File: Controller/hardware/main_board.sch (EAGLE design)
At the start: 47 parts, among them IC1 LINEAR_78DT, IC2 40XX_4050D, IC3 LP298XS, IC5 ATMEGA328, U1 CSTNE16M0VH3L000R0, X1 MICROSD_SMD, X4 CON-PHOENIX-508_MST2V

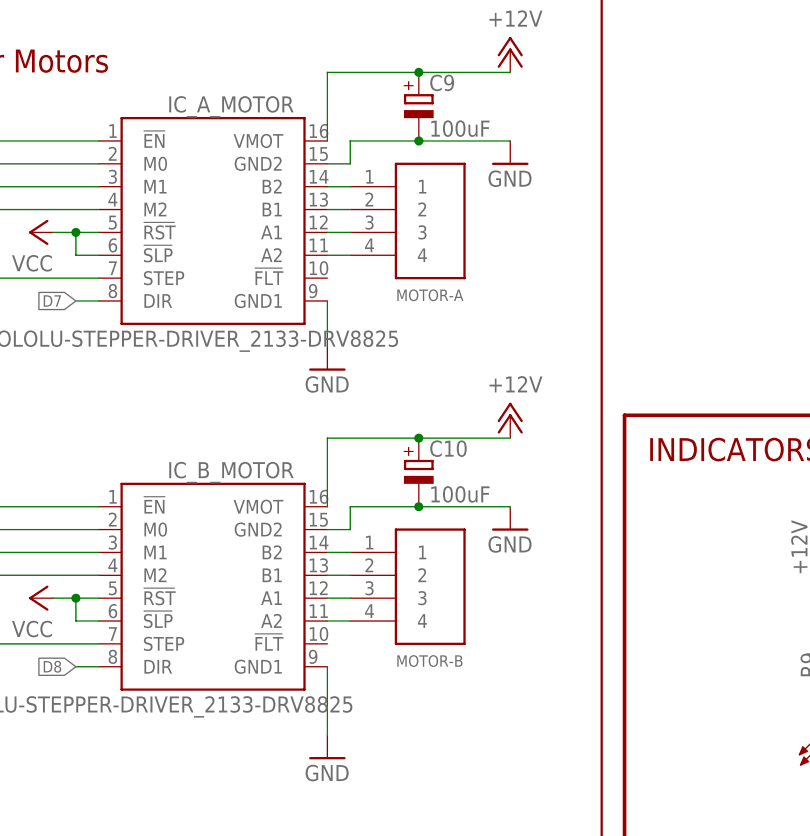
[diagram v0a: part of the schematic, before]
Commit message: changed motor connectors
changed motor connectors to .1" pitch 4 pos headers. the stepper motor stock connectors press nicely onto these. so if one wanted to they could just pins instead of soldering wires directly to the board. if soldering directly to the board the new larger pads should be more robust too.
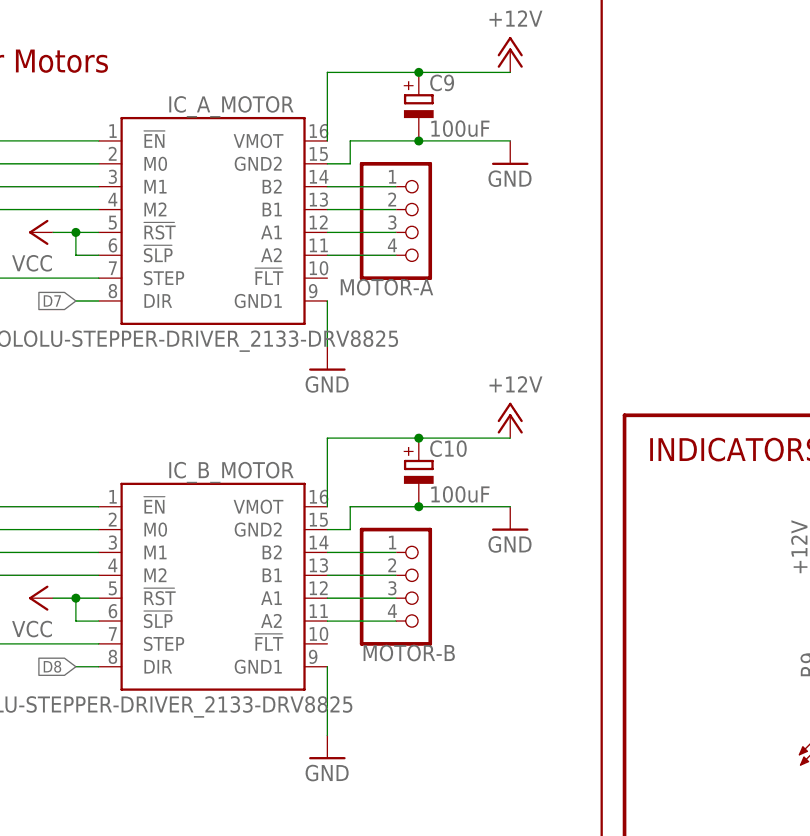
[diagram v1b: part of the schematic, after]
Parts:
- MOTOR-A, MOTOR-B: value JST_EPH_4PIN -> (none); device main_board:JST_EPH_4PIN -> main_board:PINHD-1X4
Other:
- moved on the sheet: MOTOR-A, MOTOR-B
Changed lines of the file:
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@@
 <part name="C9" library="main_board" deviceset="C100UF_EC" device="E3.5-8" value="100uF"/>
 <part name="C10" library="main_board" deviceset="C100UF_EC" device="E3.5-8" value="100uF"/>
-<part name="MOTOR-A" library="main_board" deviceset="JST_EPH_4PIN" device=""/>
-<part name="MOTOR-B" library="main_board" deviceset="JST_EPH_4PIN" device=""/>
 <part name="J1" library="main_board" deviceset="JUMPER_J2" device="X5MM"/>
 <part name="JP4" library="main_board" deviceset="JST_EPH_2PIN" device=""/>
@@
 <part name="C15" library="main_board" deviceset="C1.0UF_0805" device="0805" value="1.0uF"/>
 <part name="SUPPLY4" library="main_board" deviceset="GND" device=""/>
+<part name="MOTOR-A" library="main_board" deviceset="PINHD-1X4" device=""/>
+<part name="MOTOR-B" library="main_board" deviceset="PINHD-1X4" device=""/>
 </parts>
 <sheets>
@@
 <attribute name="VALUE" x="92.583" y="46.2026" size="1.778" layer="96"/>
 </instance>
-<instance part="MOTOR-A" gate="G$1" x="88.9" y="78.74" smashed="yes">
-<attribute name="NAME" x="88.9" y="68.58" size="1.27" layer="95"/>
-</instance>
-<instance part="MOTOR-B" gate="G$1" x="88.9" y="38.1" smashed="yes">
-<attribute name="NAME" x="88.9" y="27.94" size="1.27" layer="95"/>
-</instance>
 <instance part="J1" gate="G$1" x="287.02" y="53.34" smashed="yes" rot="R90">
 <attribute name="NAME" x="287.02" y="55.245" size="1.778" layer="95" rot="R90"/>
@@
 <instance part="SUPPLY4" gate="1" x="411.48" y="172.72" smashed="yes">
 <attribute name="VALUE" x="411.607" y="173.101" size="1.778" layer="96"/>
+</instance>
+<instance part="MOTOR-A" gate="G$1" x="91.44" y="78.74" smashed="yes">
+<attribute name="NAME" x="82.55" y="69.215" size="1.778" layer="95"/>
+<attribute name="VALUE" x="85.09" y="68.58" size="1.778" layer="96"/>
+</instance>
+<instance part="MOTOR-B" gate="G$1" x="91.44" y="38.1" smashed="yes">
+<attribute name="NAME" x="85.09" y="28.575" size="1.778" layer="95"/>
+<attribute name="VALUE" x="85.09" y="27.94" size="1.778" layer="96"/>
 </instance>
 </instances>
@@
 <pinref part="IC_A_MOTOR" gate="G$1" pin="B2"/>
 <pinref part="MOTOR-A" gate="G$1" pin="1"/>
-<wire x1="83.82" y1="81.28" x2="81.28" y2="81.28" width="0.1524" layer="91"/>
+<wire x1="81.28" y1="81.28" x2="88.9" y2="81.28" width="0.1524" layer="91"/>
 </segment>
 </net>
@@
 <pinref part="IC_A_MOTOR" gate="G$1" pin="B1"/>
 <pinref part="MOTOR-A" gate="G$1" pin="2"/>
-<wire x1="83.82" y1="78.74" x2="81.28" y2="78.74" width="0.1524" layer="91"/>
+<wire x1="81.28" y1="78.74" x2="88.9" y2="78.74" width="0.1524" layer="91"/>
 </segment>
 </net>
@@
 <pinref part="IC_A_MOTOR" gate="G$1" pin="A1"/>
 <pinref part="MOTOR-A" gate="G$1" pin="3"/>
-<wire x1="83.82" y1="76.2" x2="81.28" y2="76.2" width="0.1524" layer="91"/>
+<wire x1="81.28" y1="76.2" x2="88.9" y2="76.2" width="0.1524" layer="91"/>
 </segment>
 </net>
@@
 <pinref part="IC_A_MOTOR" gate="G$1" pin="A2"/>
 <pinref part="MOTOR-A" gate="G$1" pin="4"/>
-<wire x1="83.82" y1="73.66" x2="81.28" y2="73.66" width="0.1524" layer="91"/>
+<wire x1="81.28" y1="73.66" x2="88.9" y2="73.66" width="0.1524" layer="91"/>
 </segment>
 </net>
@@
 <pinref part="IC_B_MOTOR" gate="G$1" pin="B2"/>
 <pinref part="MOTOR-B" gate="G$1" pin="1"/>
-<wire x1="83.82" y1="40.64" x2="81.28" y2="40.64" width="0.1524" layer="91"/>
+<wire x1="88.9" y1="40.64" x2="81.28" y2="40.64" width="0.1524" layer="91"/>
 </segment>
 </net>
@@
 <pinref part="IC_B_MOTOR" gate="G$1" pin="B1"/>
 <pinref part="MOTOR-B" gate="G$1" pin="2"/>
-<wire x1="83.82" y1="38.1" x2="81.28" y2="38.1" width="0.1524" layer="91"/>
+<wire x1="88.9" y1="38.1" x2="81.28" y2="38.1" width="0.1524" layer="91"/>
 </segment>
 </net>
@@
 <pinref part="IC_B_MOTOR" gate="G$1" pin="A1"/>
 <pinref part="MOTOR-B" gate="G$1" pin="3"/>
-<wire x1="83.82" y1="35.56" x2="81.28" y2="35.56" width="0.1524" layer="91"/>
+<wire x1="88.9" y1="35.56" x2="81.28" y2="35.56" width="0.1524" layer="91"/>
 </segment>
 </net>
@@
 <pinref part="IC_B_MOTOR" gate="G$1" pin="A2"/>
 <pinref part="MOTOR-B" gate="G$1" pin="4"/>
-<wire x1="83.82" y1="33.02" x2="81.28" y2="33.02" width="0.1524" layer="91"/>
-</segment>
-</net>
+<wire x1="88.9" y1="33.02" x2="81.28" y2="33.02" width="0.1524" layer="91"/>
+</segment>
+</net>

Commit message: updated board name
updated board name while retaining the original board design files
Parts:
- removed C11: 0.1uF, main_board:C0.1UF_08050805
- removed C15: 1.0uF, main_board:C1.0UF_08050805
- removed U1: CSTNE16M0VH3L000R0, main_board:CSTNE16M0VH3L000R0
- added Q4: 16MHZ, crystal:CRYSTALHC49S
- 12V: value 12v -> (none); device main_board:LED_RED_08050805 -> SparkFun:LED0805
- ACT: value ACT -> RED; device main_board:LED_RED_08050805 -> adafruit:LEDCHIP-LED0805
- C1: value 10uF -> 10uF/10V; device main_board:C10UF_08050805 -> adafruit:CPOL-USA/3216-18R
- C10, C4, C6, C7, C9: device main_board:C100UF_ECE3.5-8 -> rcl:CPOL-EUE3.5-8
- C12: value 0.1uF -> 16pf; device main_board:C0.1UF_08050805 -> SparkFun:CAP0805
- C13: value 2.2uF -> 16pf; device main_board:C2.2UF_08050805 -> SparkFun:CAP0805
- C14, C3, C5, C8: value 0.1uF -> 100nF; device main_board:C0.1UF_08050805 -> SparkFun:CAP0805
- C2: device main_board:C0.1UF_08050805 -> adafruit:C-USC0805K
- IC1: value LINEAR_78DT -> 7805DT; device main_board:LINEAR_78DT -> linear:7805DT
- IC2: value 40XX_4050D -> 4050D; device main_board:40XX_4050D -> 40xx:4050D
- IC3: device main_board:LP298XS -> adafruit:LP298XS
- IC5: device main_board:ATMEGA328P -> SparkFun:ATMEGA168
- ICSP: device main_board:CON-HARTING-ML_ML6 -> con-harting-ml:ML6
- IC_A_MOTOR, IC_B_MOTOR: value POLOLU-STEPPER-DRIVER_2133-DRV8825 -> 2133-DRV8825; device main_board:POLOLU-STEPPER-DRIVER_2133-DRV8825 -> pololu-stepper-driver:2133-DRV8825
- J1: device main_board:JUMPER_J2X5MM -> jumper:J2X5MM
- JP1, JP5: device main_board:ADAFRUIT_PINHD-1X3 -> adafruit:PINHD-1X3
- JP4: value JST_EPH_2PIN -> 2PIN; device main_board:JST_EPH_2PIN -> jst_eph:2PIN
- MOTOR-A, MOTOR-B: value (none) -> 4PIN; device main_board:PINHD-1X4 -> jst_eph:4PIN
- R1: value 1.0k -> 1K; device main_board:R1.0K_0805R0805 -> adafruit:R-US_R0805
- R10: value 330 -> 330r; device main_board:R330_0805R0805 -> adafruit:R-US_R0805
- R2, R3: value 10k -> 10K; device main_board:R10K_0805R0805 -> adafruit:R-US_R0805
- R7: value 10k -> 10K; device main_board:R10K_0805R0805 -> SparkFun:RESISTOR
- R9: value 2.2k -> 2.2K; device main_board:R2.2K_0805R0805 -> SparkFun:RESISTOR
- SJ1, SJ2, SJ3, SJ4, SJ5, SJ6: device main_board:JUMPER_SJ -> jumper:SJ
- SW_NEXT: device main_board:TACT_SW_EVQQ2-EVQQ2 -> adafruit:SPST_TACT-EVQQ2
- U$1: value DIY-MODULES_DISPLAY-OLED-128X64-I2C -> DISPLAY-OLED-128X64-I2C; device main_board:DIY-MODULES_DISPLAY-OLED-128X64-I2C -> diy-modules:DISPLAY-OLED-128X64-I2C
- X1: value MICROSD_SMD -> MICROSD; device main_board:MICROSD_SMD -> adafruit:MICROSD
- X4: value CON-PHOENIX-508_MST2V -> MST2V; device main_board:CON-PHOENIX-508_MST2V -> con-phoenix-508:MST2V
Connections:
- removed net N$22: IC5.PB6(XTAL1/TOSC1), U1.IN
- removed net N$23: IC5.PB7(XTAL2/TOSC2), U1.OUT
- new net N$31: C12.2, IC5.PB6(XTAL1/TOSC1), Q4.2
- new net N$32: C13.2, IC5.PB7(XTAL2/TOSC2), Q4.1
- net +3V3: now also C1.+; no longer C1.1, C13.2, C2.1
- net GND: now also C1.-; no longer C1.2, C11.1, C15.2, U1.GND
- net VCC: now also C2.1; no longer C11.2, C12.2, C15.1
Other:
- moved on the sheet: 12V, ACT, C10, C12, C13, C14, C2, C3, C4, C5, C6, C7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
